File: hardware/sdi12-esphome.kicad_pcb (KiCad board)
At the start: 2 copper layers, 92.8 x 74 mm, 30 parts, among them J0 Grounding, J1 SDI-12 A, J2 SDI-12 B, J3 SDI-12 C, J4 SDI-12 D, J5 GPIO21/22, J6 Rain Gauge, Q1 2N7002, U1 ESP32_NODEMCU, U2 74LVC1G125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

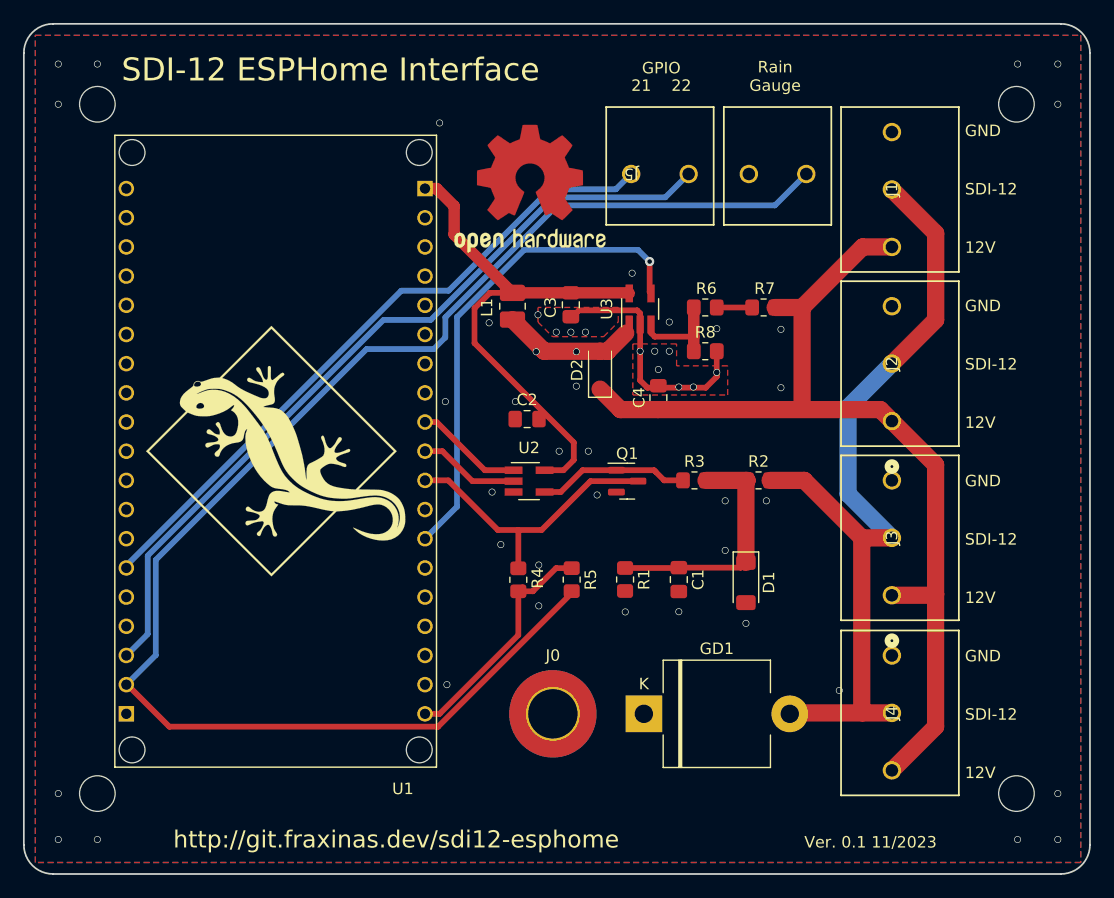
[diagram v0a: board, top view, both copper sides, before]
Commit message: board: Implement LED, re-arrange snubber and boost converter
* also fix some DRC problems
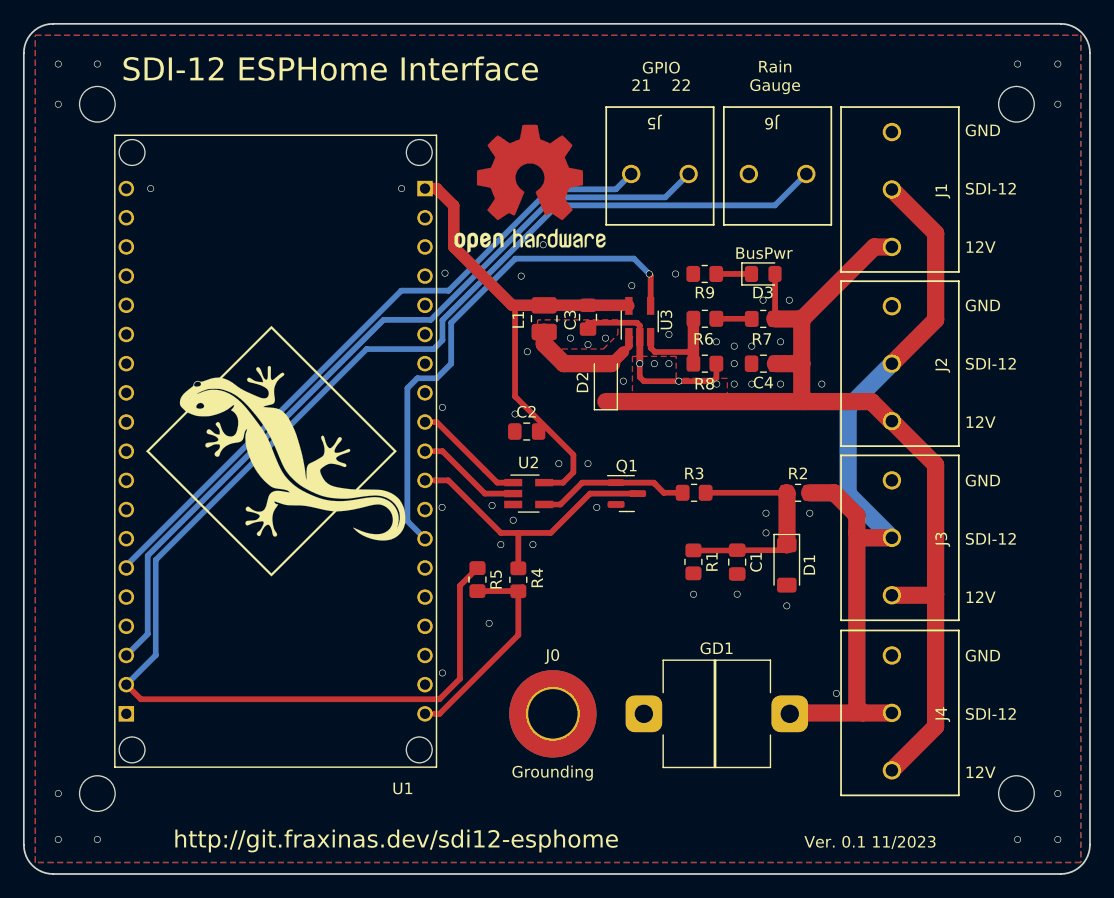
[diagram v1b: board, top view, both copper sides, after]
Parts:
- added D3: LED, LED_SMD:LED_0805_2012Metric_Pad1.15x1.40mm_HandSolder, F.Cu at (103.4, 60.8)
- added R9: 510R, Resistor_SMD:R_0805_2012Metric_Pad1.20x1.40mm_HandSolder, F.Cu at (98.3, 60.8)
- GD1: value GDT_2Pin -> 10kV 90V; footprint Diode_THT:D_P600_R-6_P12.70mm_Horizontal -> Fraxinas-kicad:Gas Discharge Tube Generic 12.7mm THT
- J2, J3, J4: footprint Fraxinas-kicad:Phoenix Contact SPTA 1 3 3,5 1752227 -> Fraxinas-kicad:Phoenix Contact SPTA 1 3 5,0 1752227
- moved C4 9.61 mm to (103.4, 68.6), turned to 180 degrees
- moved R5 8.20 mm to (78.5, 87.4), turned to 90 degrees
- moved R1 6.14 mm to (97.3, 85.8)
- moved C1 5.30 mm to (101.1, 85.9)
- moved D1 3.87 mm to (105.4, 86.1)
- moved R2 3.61 mm to (106.4, 79.8)
- moved L1 2.97 mm to (84.3, 64.7)
- moved C3 1.84 mm to (88.1, 64.5)
- moved D2 1.20 mm to (89.7, 70.2)
- moved Q1 1.08 mm to (91.5, 79.9)
- moved R3 1.08 mm to (97.3, 79.8)
- moved U2 1.08 mm to (82.9, 79.9)
- moved U3 1.08 mm to (92.6, 64.9)
- moved C2 1.08 mm to (82.8, 74.5)
- moved R8 1.08 mm to (98.3, 68.6)
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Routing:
- net GPIO23: track 128.8 -> 124.1 mm
- net +12V: track 85.1 -> 89.3 mm
- net GND: track 21.4 -> 17.8 mm, vias 50 -> 60
- net Net-(D3-K): track 0.00 -> 3.07 mm
- net +5V: track 46.6 -> 43.7 mm
- net SDI12_Bus: track 73.4 -> 71.0 mm
- net VCC Enable: track 42.9 -> 44.9 mm
- net +3V3: track 20.8 -> 19.0 mm
- net Net-(D1-K): track 21.5 -> 19.9 mm
- net Net-(D2-A): track 11.7 -> 10.6 mm
- net RXD: track 25.4 -> 24.9 mm
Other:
- board text added: "BusPwr"
